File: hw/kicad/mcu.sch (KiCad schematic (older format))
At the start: 7 parts

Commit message: First steps on gate driver circuit
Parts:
- added C? (x2): 100n, symbol C
- added P?: CONN_01X05, symbol CONN_01X05
- added Y?: 16 MHz, symbol Crystal
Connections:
- net labels added: +3.3V, DC_CAL, EN_GATE, GNDD, I_SENS_A, I_SENS_B, I_SENS_V_REF, PWM_H_A, PWM_H_B, PWM_H_C, PWM_L_A, PWM_L_B, PWM_L_C, SPI_CLK, SPI_CS, SPI_MISO, SPI_MOSI, nFAULT, nOCTW
- net labels removed: GND, VDD
- wire segments 27 -> 49
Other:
- note added: "C load = 9 pF"
- moved on the sheet: C?

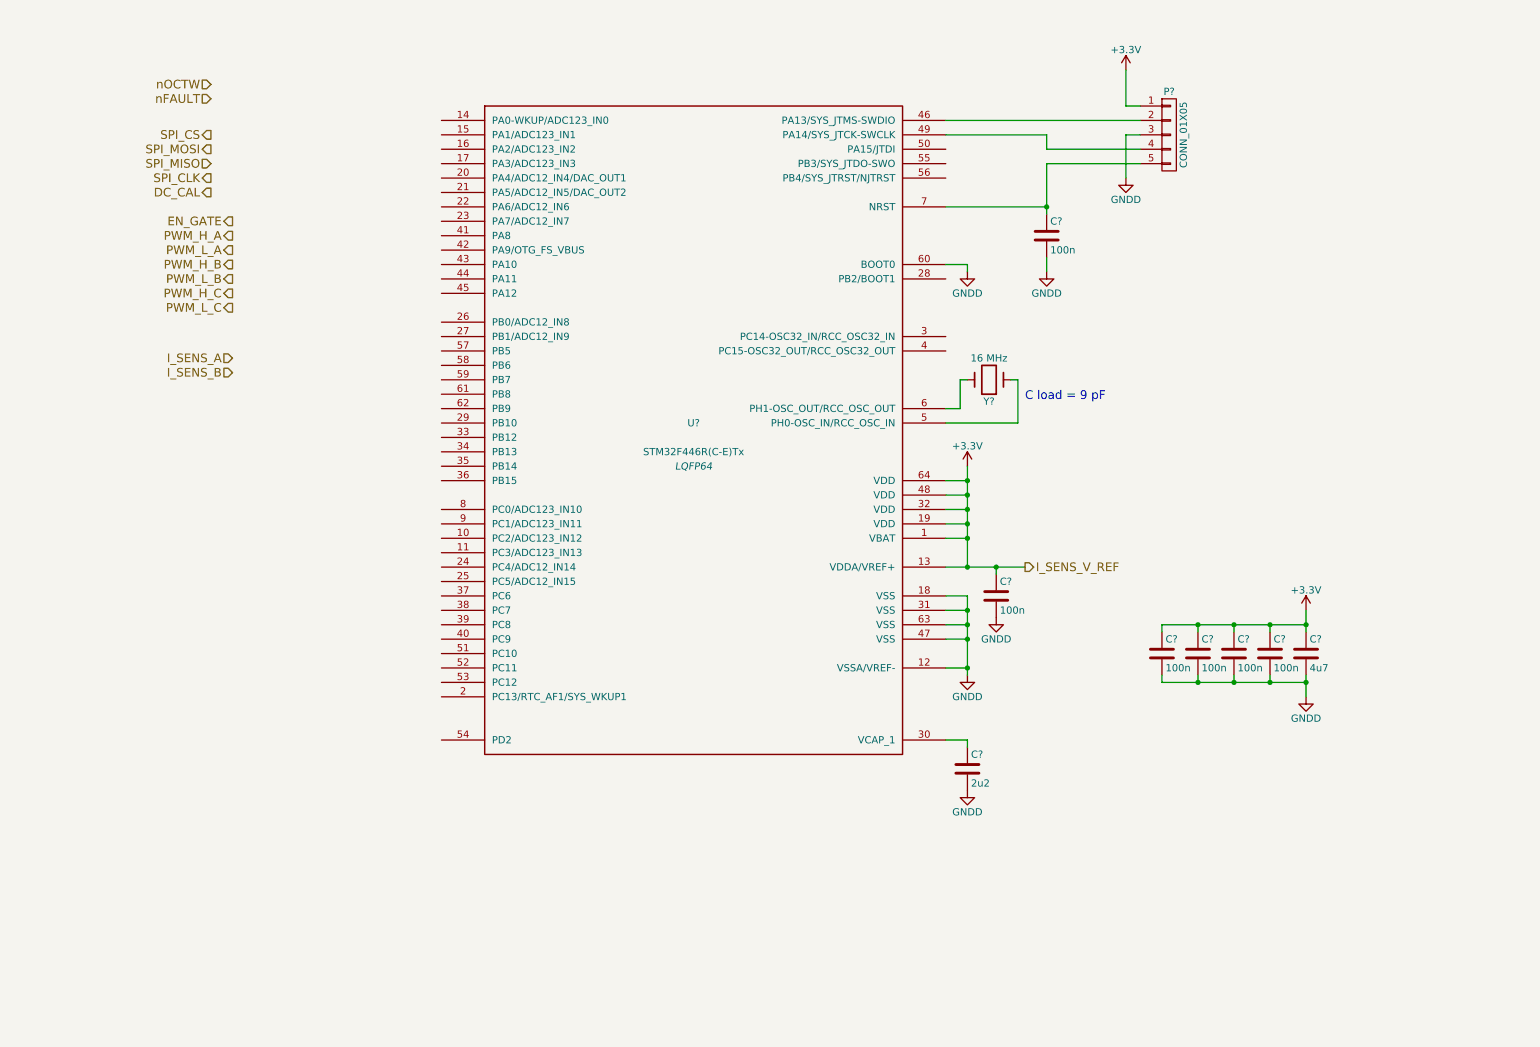
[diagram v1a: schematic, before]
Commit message: Added power mosfet footprint
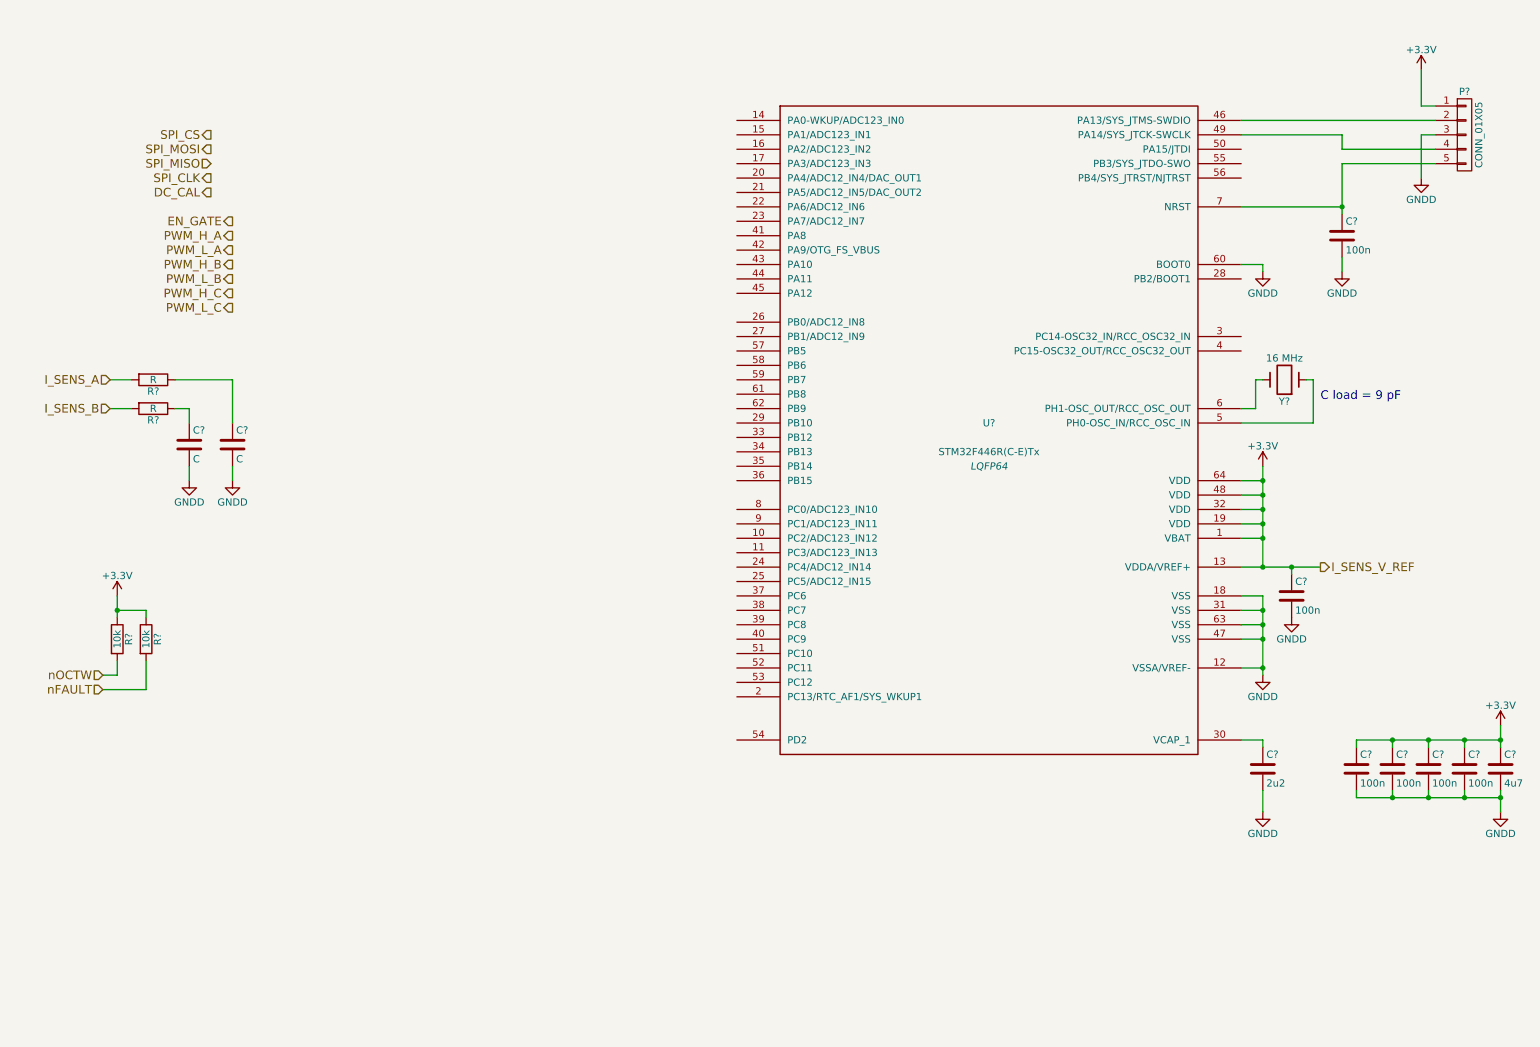
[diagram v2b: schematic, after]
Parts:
- added C? (x2): C, symbol C
- added R? (x2): 10k, symbol R
- added R? (x2): R, symbol R
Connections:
- net +3V3: now also R?.1, R?.1
- net GNDD: now also C?.2, C?.2
- net I_SENS_A: now also R?.2
- net I_SENS_B: now also R?.2
- net nFAULT: now also R?.2
- net nOCTW: now also R?.2
- new net: C?.1, R?.1 (x2)
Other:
- moved on the sheet: C?, P?, U?, Y?

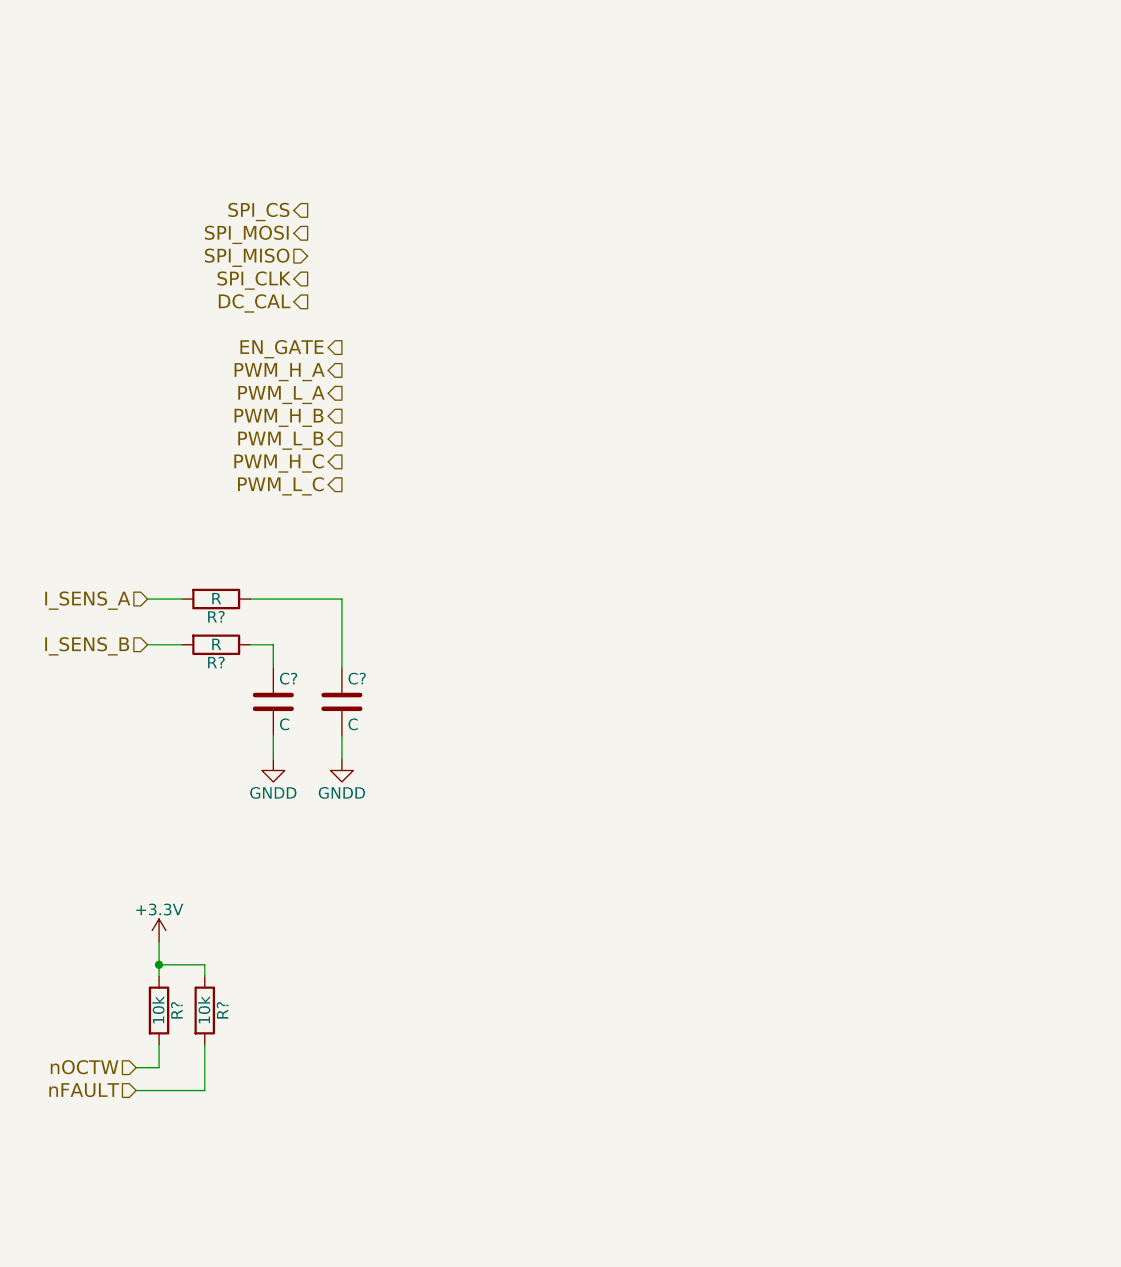
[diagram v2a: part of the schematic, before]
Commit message: Some more work on the FET-stage
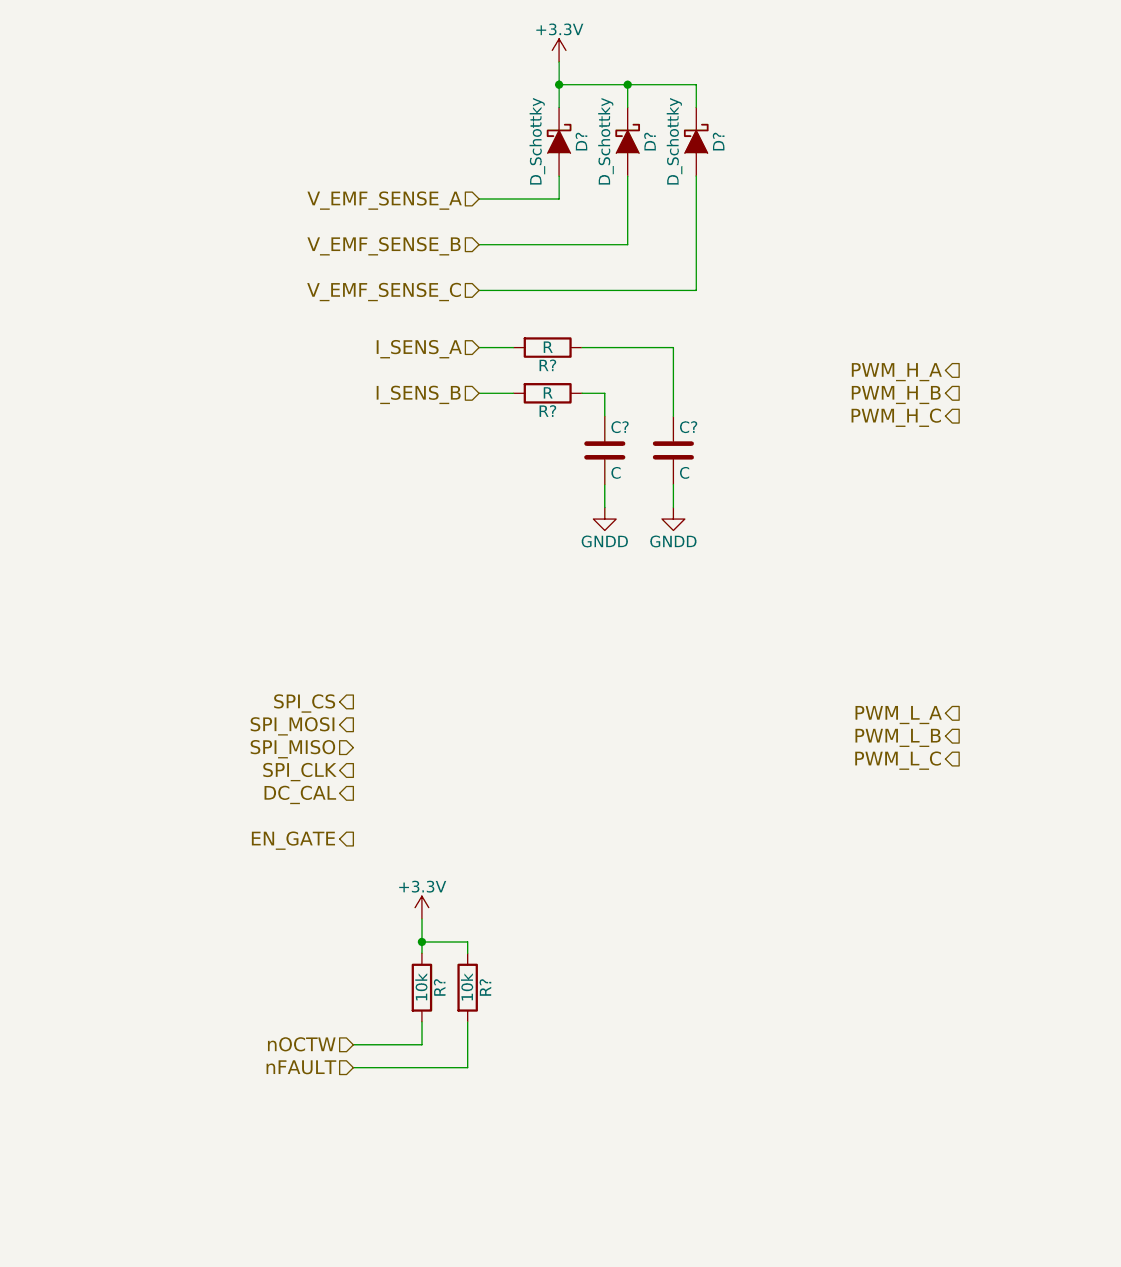
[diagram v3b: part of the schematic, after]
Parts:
- added D? (x3): D_Schottky, symbol D_Schottky
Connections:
- net +3V3: now also D?.1 (K), D?.1 (K), D?.1 (K)
- new net V_EMF_SENSE_A: D?.2 (A)
- new net V_EMF_SENSE_B: D?.2 (A)
- new net V_EMF_SENSE_C: D?.2 (A)
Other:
- moved on the sheet: C?, R?

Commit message: More power work
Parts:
- added C? (x2): np, symbol C
- added D?: D_Schottky, symbol D_Schottky
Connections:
- net +3V3: now also D?.1 (K)
- net GNDD: now also C?.1, C?.1
- net at U?.5 (PH0-OSC_IN/RCC_OSC_IN): now also Y?.2, C?.2; no longer Y?.1
- net at U?.6 (PH1-OSC_OUT/RCC_OSC_OUT): now also Y?.1, C?.2; no longer Y?.2
- new net V_BAT_SENSE: D?.2 (A)
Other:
- moved on the sheet: C?, R?, Y?
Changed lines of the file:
@@
 LIBS:Zilog
 LIBS:drv8301
+LIBS:wslp2726
+LIBS:test
 LIBS:MotCtrl-cache
 EELAYER 25 0
@@
 Text HLabel 9550 4400 2    60   Output ~ 0
 I_SENS_V_REF
-Text HLabel 2600 2000 0    60   Input ~ 0
+Text HLabel 2600 2450 0    60   Input ~ 0
 I_SENS_A
-Text HLabel 2600 2200 0    60   Input ~ 0
+Text HLabel 2600 2650 0    60   Input ~ 0
 I_SENS_B
 $Comp
@@
 L Crystal Y?
 U 1 1 5817878B
-P 9300 3100
-F 0 "Y?" H 9300 3250 50  0000 C CNN
-F 1 "16 MHz" H 9300 2950 50  0000 C CNN
-F 2 "" H 9300 3100 60  0000 C CNN
-F 3 "" H 9300 3100 60  0000 C CNN
-	1    9300 3100
-	-1   0    0    1
-$EndComp
-Wire Wire Line
-	9000 3300 9100 3300
-Wire Wire Line
-	9100 3300 9100 3100
-Wire Wire Line
-	9100 3100 9150 3100
-Wire Wire Line
-	9000 3400 9500 3400
-Wire Wire Line
-	9500 3400 9500 3100
-Wire Wire Line
-	9500 3100 9450 3100
-Text Notes 9550 3250 0    60   ~ 0
+P 9700 3350
+F 0 "Y?" V 9700 3500 50  0000 C CNN
+F 1 "16 MHz" H 9700 3200 50  0000 C CNN
+F 2 "" H 9700 3350 60  0000 C CNN
+F 3 "" H 9700 3350 60  0000 C CNN
+	1    9700 3350
+	0    1    1    0
+$EndComp
+Text Notes 9300 3100 0    60   ~ 0
 C load = 9 pF
 $Comp
@@
 L R R?
 U 1 1 5817D266
-P 2900 2200
-F 0 "R?" V 2980 2200 50  0000 C CNN
-F 1 "R" V 2900 2200 50  0000 C CNN
-F 2 "" V 2830 2200 30  0000 C CNN
-F 3 "" H 2900 2200 30  0000 C CNN
-	1    2900 2200
+P 2900 2650
+F 0 "R?" V 2980 2650 50  0000 C CNN
+F 1 "R" V 2900 2650 50  0000 C CNN
+F 2 "" V 2830 2650 30  0000 C CNN
+F 3 "" H 2900 2650 30  0000 C CNN
+	1    2900 2650
 	0    1    1    0
 $EndComp
@@
 L C C?
 U 1 1 5817D2BF
-P 3150 2450
-F 0 "C?" H 3175 2550 50  0000 L CNN
-F 1 "C" H 3175 2350 50  0000 L CNN
-F 2 "" H 3188 2300 30  0000 C CNN
-F 3 "" H 3150 2450 60  0000 C CNN
-	1    3150 2450
-	1    0    0    -1
-$EndComp
-Wire Wire Line
-	2600 2200 2750 2200
-Wire Wire Line
-	3050 2200 3150 2200
-Wire Wire Line
-	3150 2200 3150 2300
+P 3150 2900
+F 0 "C?" H 3175 3000 50  0000 L CNN
+F 1 "C" H 3175 2800 50  0000 L CNN
+F 2 "" H 3188 2750 30  0000 C CNN
+F 3 "" H 3150 2900 60  0000 C CNN
+	1    3150 2900
+	1    0    0    -1
+$EndComp
+Wire Wire Line
+	2600 2650 2750 2650
+Wire Wire Line
+	3050 2650 3150 2650
+Wire Wire Line
+	3150 2650 3150 2750
 $Comp
 L GNDD #PWR?
 U 1 1 5817D404
-P 3150 2700
-F 0 "#PWR?" H 3150 2450 50  0001 C CNN
-F 1 "GNDD" H 3150 2550 50  0000 C CNN
-F 2 "" H 3150 2700 60  0000 C CNN
-F 3 "" H 3150 2700 60  0000 C CNN
-	1    3150 2700
-	1    0    0    -1
-$EndComp
-Wire Wire Line
-	3150 2700 3150 2600
+P 3150 3150
+F 0 "#PWR?" H 3150 2900 50  0001 C CNN
+F 1 "GNDD" H 3150 3000 50  0000 C CNN
+F 2 "" H 3150 3150 60  0000 C CNN
+F 3 "" H 3150 3150 60  0000 C CNN
+	1    3150 3150
+	1    0    0    -1
+$EndComp
+Wire Wire Line
+	3150 3150 3150 3050
 $Comp
 L R R?
 U 1 1 5817D4F7
-P 2900 2000
-F 0 "R?" V 2980 2000 50  0000 C CNN
-F 1 "R" V 2900 2000 50  0000 C CNN
-F 2 "" V 2830 2000 30  0000 C CNN
-F 3 "" H 2900 2000 30  0000 C CNN
-	1    2900 2000
-	0    1    1    0
-$EndComp
-Wire Wire Line
-	2600 2000 2750 2000
+P 2900 2450
+F 0 "R?" V 2980 2450 50  0000 C CNN
+F 1 "R" V 2900 2450 50  0000 C CNN
+F 2 "" V 2830 2450 30  0000 C CNN
+F 3 "" H 2900 2450 30  0000 C CNN
+	1    2900 2450
+	0    1    1    0
+$EndComp
+Wire Wire Line
+	2600 2450 2750 2450
 $Comp
 L C C?
 U 1 1 5817D614
-P 3450 2450
-F 0 "C?" H 3475 2550 50  0000 L CNN
-F 1 "C" H 3475 2350 50  0000 L CNN
-F 2 "" H 3488 2300 30  0000 C CNN
-F 3 "" H 3450 2450 60  0000 C CNN
-	1    3450 2450
-	1    0    0    -1
-$EndComp
-Wire Wire Line
-	3450 2000 3450 2300
-Wire Wire Line
-	3050 2000 3450 2000
+P 3450 2900
+F 0 "C?" H 3475 3000 50  0000 L CNN
+F 1 "C" H 3475 2800 50  0000 L CNN
+F 2 "" H 3488 2750 30  0000 C CNN
+F 3 "" H 3450 2900 60  0000 C CNN
+	1    3450 2900
+	1    0    0    -1
+$EndComp
+Wire Wire Line
+	3450 2450 3450 2750
+Wire Wire Line
+	3050 2450 3450 2450
 $Comp
 L GNDD #PWR?
 U 1 1 5817D6CF
-P 3450 2700
-F 0 "#PWR?" H 3450 2450 50  0001 C CNN
-F 1 "GNDD" H 3450 2550 50  0000 C CNN
-F 2 "" H 3450 2700 60  0000 C CNN
-F 3 "" H 3450 2700 60  0000 C CNN
-	1    3450 2700
-	1    0    0    -1
-$EndComp
-Wire Wire Line
-	3450 2700 3450 2600
+P 3450 3150
+F 0 "#PWR?" H 3450 2900 50  0001 C CNN
+F 1 "GNDD" H 3450 3000 50  0000 C CNN
+F 2 "" H 3450 3150 60  0000 C CNN
+F 3 "" H 3450 3150 60  0000 C CNN
+	1    3450 3150
+	1    0    0    -1
+$EndComp
+Wire Wire Line
+	3450 3150 3450 3050
 Wire Wire Line
 	9150 6100 9150 5950
@@
 	3550 1750 3550 1250
 Wire Wire Line
-	2950 850  3550 850
+	2950 850  3850 850
 Wire Wire Line
 	3550 850  3550 950
@@
 	3250 950  3250 850
 Connection ~ 3250 850
+$Comp
+L C C?
+U 1 1 581E8136
+P 10050 3550
+F 0 "C?" V 10200 3500 50  0000 L CNN
+F 1 "np" V 10000 3600 50  0000 L CNN
+F 2 "" H 10088 3400 30  0000 C CNN
+F 3 "" H 10050 3550 60  0000 C CNN
+	1    10050 3550
+	0    1    1    0
+$EndComp
+Wire Wire Line
+	9000 3300 9400 3300
+Wire Wire Line
+	9400 3300 9400 3150
+Wire Wire Line
+	9400 3150 9900 3150
+Wire Wire Line
+	9700 3150 9700 3200
+Wire Wire Line
+	9700 3500 9700 3550
+Wire Wire Line
+	9400 3550 9900 3550
+Wire Wire Line
+	9400 3550 9400 3400
+Wire Wire Line
+	9400 3400 9000 3400
+$Comp
+L C C?
+U 1 1 581E851F
+P 10050 3150
+F 0 "C?" V 10200 3100 50  0000 L CNN
+F 1 "np" V 10000 3200 50  0000 L CNN
+F 2 "" H 10088 3000 30  0000 C CNN
+F 3 "" H 10050 3150 60  0000 C CNN
+	1    10050 3150
+	0    1    1    0
+$EndComp
+Connection ~ 9700 3150
+Connection ~ 9700 3550
+$Comp
+L GNDD #PWR?
+U 1 1 581E869D
+P 10450 3400
+F 0 "#PWR?" H 10450 3150 50  0001 C CNN
+F 1 "GNDD" H 10450 3250 50  0000 C CNN
+F 2 "" H 10450 3400 60  0000 C CNN
+F 3 "" H 10450 3400 60  0000 C CNN
+	1    10450 3400
+	1    0    0    -1
+$EndComp
+Wire Wire Line
+	10200 3150 10300 3150
+Wire Wire Line
+	10300 3150 10300 3550
+Wire Wire Line
+	10300 3350 10450 3350
+Wire Wire Line
+	10450 3350 10450 3400
+Wire Wire Line
+	10300 3550 10200 3550
+Connection ~ 10300 3350
+Text HLabel 2600 1950 0    60   Input ~ 0
+V_BAT_SENSE
+$Comp
+L D_Schottky D?
+U 1 1 581EDE1A
+P 3850 1100
+F 0 "D?" H 3850 1200 50  0000 C CNN
+F 1 "D_Schottky" H 3850 1000 50  0000 C CNN
+F 2 "" H 3850 1100 60  0000 C CNN
+F 3 "" H 3850 1100 60  0000 C CNN
+	1    3850 1100
+	0    1    1    0
+$EndComp
+Wire Wire Line
+	2600 1950 3850 1950
+Wire Wire Line
+	3850 1950 3850 1250
+Wire Wire Line
+	3850 850  3850 950
+Connection ~ 3550 850
 $EndSCHEMATC
